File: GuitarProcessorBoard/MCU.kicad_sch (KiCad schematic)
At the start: 93 parts, among them J301 SWD Header, J302 PWR, J304 MODE, J305 BYP, J307 ScopeGroundLoop, SW301 RST, SW302 BOOT, U1 AMS1117, U301 STM32H7B0VBT6, U302 TPS63070, U303 SSD1306_OLED_128x64, U304 74HC595, Y301 32MHz, Y302 32.768kHZ

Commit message: migrated to new cube MX version, flashing on new board works
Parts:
- R314: value 5k1 -> 15k
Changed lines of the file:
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@@
 			)
 		)
-		(property "Value" "5k1"
+		(property "Value" "15k"
 			(at 249.555 241.3 0)
 			(effects

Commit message: updated schematic, re-annotated
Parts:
- removed C315, C317: 6p, Capacitor_SMD:C_0805_2012Metric, symbol Device:C
- removed C332: 100n, Capacitor_SMD:C_0805_2012Metric, symbol Device:C
- removed J302: PWR, Connector_PinHeader_2.54mm:PinHeader_1x04_P2.54mm_Vertical, symbol Connector:Conn_01x04_Pin
- removed R303, R304: 2k2, Resistor_SMD:R_0805_2012Metric, symbol Device:R_US
- removed U303: SSD1306_OLED_128x64, Display:SSD1306_OLED_128x64_OffBoard, symbol Display_Graphic:SSD1306_OLED_128x64
- removed Y302: 32.768kHZ, Crystal:Crystal_SMD_SeikoEpson_MC306-4Pin_8.0x3.2mm, symbol Device:Crystal_GND23
- added C37: 330u, Capacitor_THT:CP_Radial_D5.0mm_P2.50mm, symbol Device:C_Polarized_US
- added C48, C52: 10n, Capacitor_SMD:C_0805_2012Metric, symbol Device:C
- added J2: IO, Connector_PinHeader_2.54mm:PinHeader_1x06_P2.54mm_Vertical, symbol Connector:Conn_01x06_Pin
- added R24, R25, R39, R41: 47k, Resistor_SMD:R_0805_2012Metric, symbol Device:R_US
- added R36, R40: 22k, Resistor_SMD:R_0805_2012Metric, symbol Device:R_US
- added RV3, RV5: 100kB, Potentiometer_THT:Potentiometer_Alpha_RD901F-40-00D_Single_Vertical_CircularHoles, symbol Device:R_Potentiometer_US
- added SW3: SW_1, Button_Switch_THT:MiniToggle_SPST, symbol Switch:SW_SPST
- added SW4: SW_2, Button_Switch_THT:MiniToggle_SPST, symbol Switch:SW_SPST
- added TP4: OutL, TestPoint:TestPoint_THTPad_D2.0mm_Drill1.0mm_VAL, symbol Connector:TestPoint
- added TP5: OutR, TestPoint:TestPoint_THTPad_D2.0mm_Drill1.0mm_VAL, symbol Connector:TestPoint
- added TP7: DB1, TestPoint:TestPoint_THTPad_D2.0mm_Drill1.0mm_VAL, symbol Connector:TestPoint
- added TP8: DB2, TestPoint:TestPoint_THTPad_D2.0mm_Drill1.0mm_VAL, symbol Connector:TestPoint
- TP1: renamed from TP301; value In -> InL
- TP2: renamed from TP302; value Out -> InR
- renumbered C318 to C23, C301 to C24, C303 to C25, C302 to C26, C333 to C27, C304 to C28, C306 to C29, C307 to C30, C308 to C31, C309 to C32, C310 to C33, C311 to C34, C312 to C35, C313 to C36, C314 to C38, C2 to C39, C4 to C40, C3 to C41, C5 to C42, C6 to C43, C7 to C44, C329 to C45, C327 to C46, C319 to C47, C328 to C49, C321 to C50, C322 to C51, C323 to C53, C324 to C54, C326 to C55, C1 to C56, D304 to D1, D301 to D2, D307 to D3, D308 to D4, D309 to D5, D310 to D6, D311 to D7, D312 to D8, D302 to D9, J301 to J1, J307 to J3, J304 to J4, J305 to J5, L301 to L1, R309 to R21, R310 to R22, R305 to R23, R331 to R26, R333 to R27, R332 to R28, R330 to R29, R301 to R30, R302 to R31, R327 to R32, R328 to R33, R317 to R34, R315 to R35, R316 to R37, R311 to R38, R312 to R42, R313 to R43, R314 to R44, R306 to R45, R307 to R46, R308 to R47, R322 to R48, R323 to R49, R324 to R50, R325 to R51, R318 to R52, RV303 to RV1, RV301 to RV2, RV302 to RV4, SW301 to SW1, SW302 to SW2, TP303 to TP3, TP1 to TP6, U304 to U4, U301 to U5, U1 to U6, U302 to U7, Y301 to Y1
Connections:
- net +3.3V: now also R24.1, R25.1, RV3.3, RV5.3, SW3.2 (B), SW4.2 (B)
- net +9V: now also J2.5 (Pin_5)
- net GND: now also C37.2, C48.2, C52.2, J2.6 (Pin_6), R39.2, R41.2, RV3.1, RV5.1
- net VCC: now also C37.1
- net ADC_D: now reaches U5.22 (PA0)
- net ADC_D: now also C48.1, R36.2
- net ADC_E: now reaches U5.25 (PA3)
- net ADC_E: now also C52.1, R40.2
- net DBG1: now reaches U5.37 (PE7)
- net DBG1: now also R25.2, TP7.1
- net DBG2: now reaches U5.38 (PE8)
- net DBG2: now also R24.2, TP8.1
- net SWITCH2: now reaches U5.65 (PC8)
- net SWITCH2: now also R41.1, SW4.1 (A)
- net SWITCH1: now reaches U5.66 (PC9)
- net SWITCH1: now also R39.1, SW3.1 (A)
- net DISP_SCL: no longer names the net of U5.92 (PB6)
- net DISP_SDA: no longer names the net of U5.93 (PB7)
- net FX_IN renamed IN_L
- net IN_L: now also J2.3 (Pin_3)
- net FX_OUT renamed IN_R
- net IN_R: now also J2.4 (Pin_4)
- net LFE_IN: no longer names the net of U5.9 (PC15)
- net LFE_OUT: no longer names the net of U5.8 (PC14)
- new net: R40.1, RV5.2
- new net: R36.1, RV3.2
- new net OUT_L: J2.1 (Pin_1), TP4.1
- new net OUT_R: J2.2 (Pin_2), TP5.1
- no-connect marks 57 -> 55
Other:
- note removed: "LFE Crystal"
- moved on the sheet: C40, C42, C43, C44, C47, C50, C51, C53, C54, C55, C56, D1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

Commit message: new layout
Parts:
- removed C23: 100n, Capacitor_SMD:C_0805_2012Metric, symbol Device:C
- removed C38: 2u2, Capacitor_SMD:C_0805_2012Metric, symbol Device:C
- removed C39: 10u, Capacitor_SMD:C_0805_2012Metric, symbol Device:C
- removed C52: 10n, Capacitor_SMD:C_0805_2012Metric, symbol Device:C
- removed R24, R25, R41: 47k, Resistor_SMD:R_0805_2012Metric, symbol Device:R_US
- removed R40: 22k, Resistor_SMD:R_0805_2012Metric, symbol Device:R_US
- removed RV5: 100kB, Potentiometer_THT:Potentiometer_Alpha_RD901F-40-00D_Single_Vertical_CircularHoles, symbol Device:R_Potentiometer_US
- removed SW2: BOOT, Button_Switch_SMD:SW_SPST_B3U-1000P, symbol Switch:SW_SPST
- removed SW4: SW_2, Button_Switch_THT:MiniToggle_SPST, symbol Switch:SW_SPST
- J3: footprint Connector:THT_GND_WIRE -> Capacitor_THT:THT_GND_WIRE
- U7: footprint Package_DFN_QFN:TXN_QFN15 -> Converter_DCDC:TXN_QFN15
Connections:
- net DBG1: now also U5.82 (PD1); no longer U5.37 (PE7)
- net DBG2: now also U5.83 (PD2); no longer U5.38 (PE8)
- net LED_BYPASS: now also U4.6 (QG); no longer U4.7 (QH)
- net LED_TEMPO: now also U4.7 (QH); no longer U4.6 (QG)
- net ADC_E: no longer names the net of U5.25 (PA3)
- net SWITCH2: no longer names the net of U5.65 (PC8)
- no-connect marks 55 -> 57
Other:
- moved on the sheet: C41, SW1

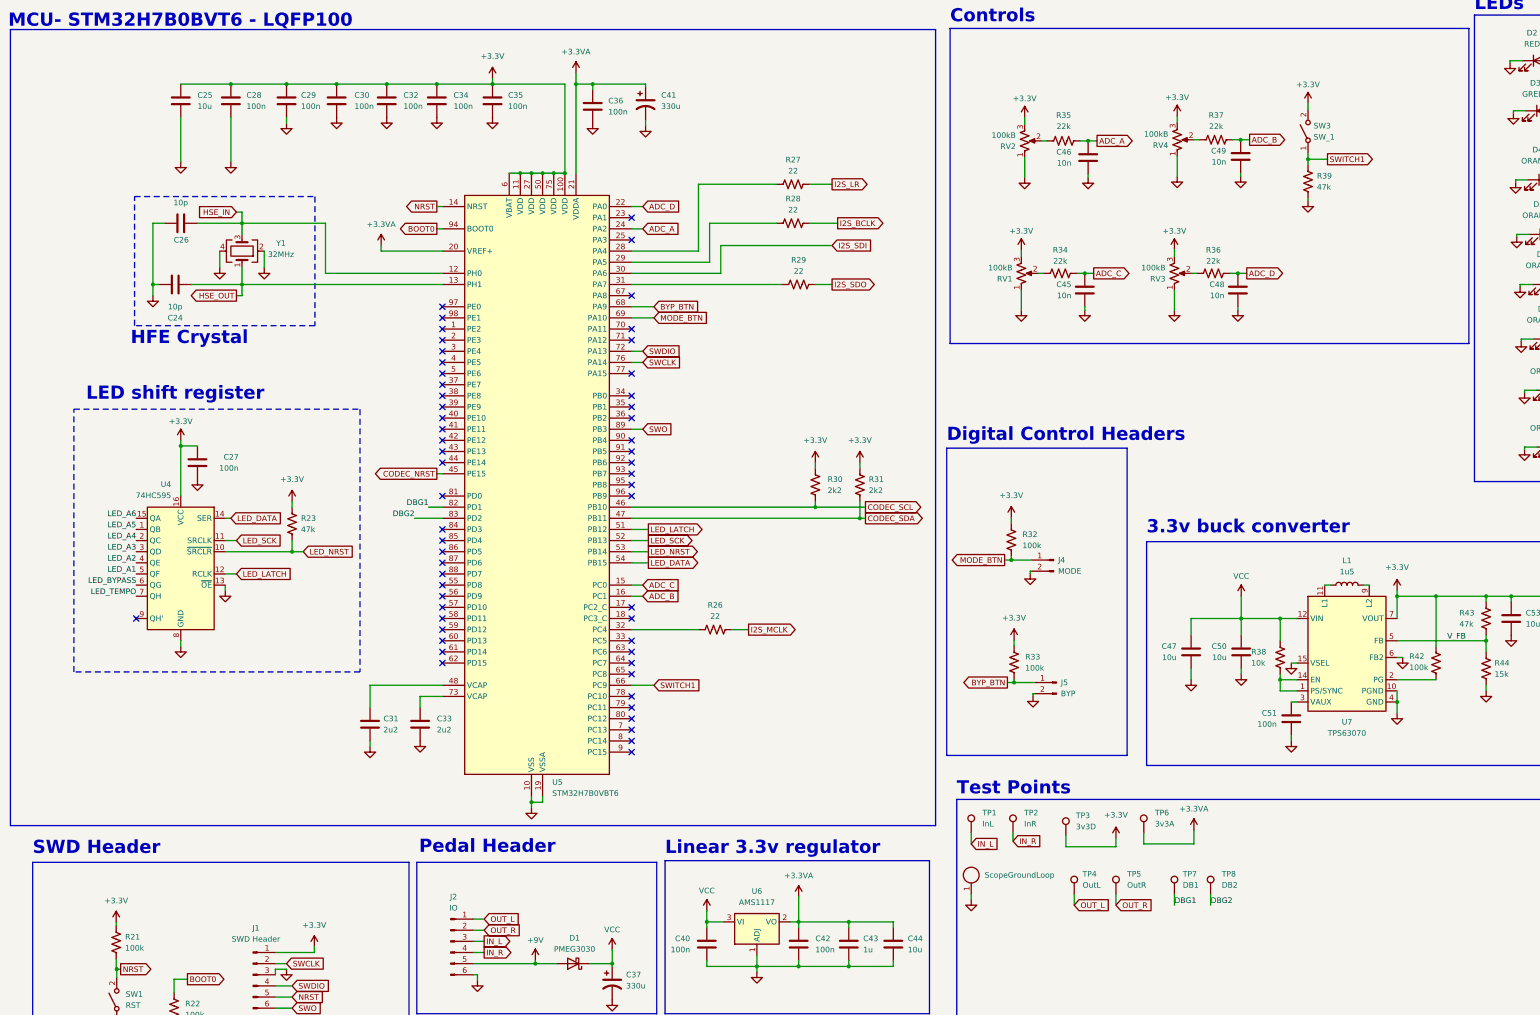
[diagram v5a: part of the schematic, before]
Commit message: prelim. routing, DRC passing
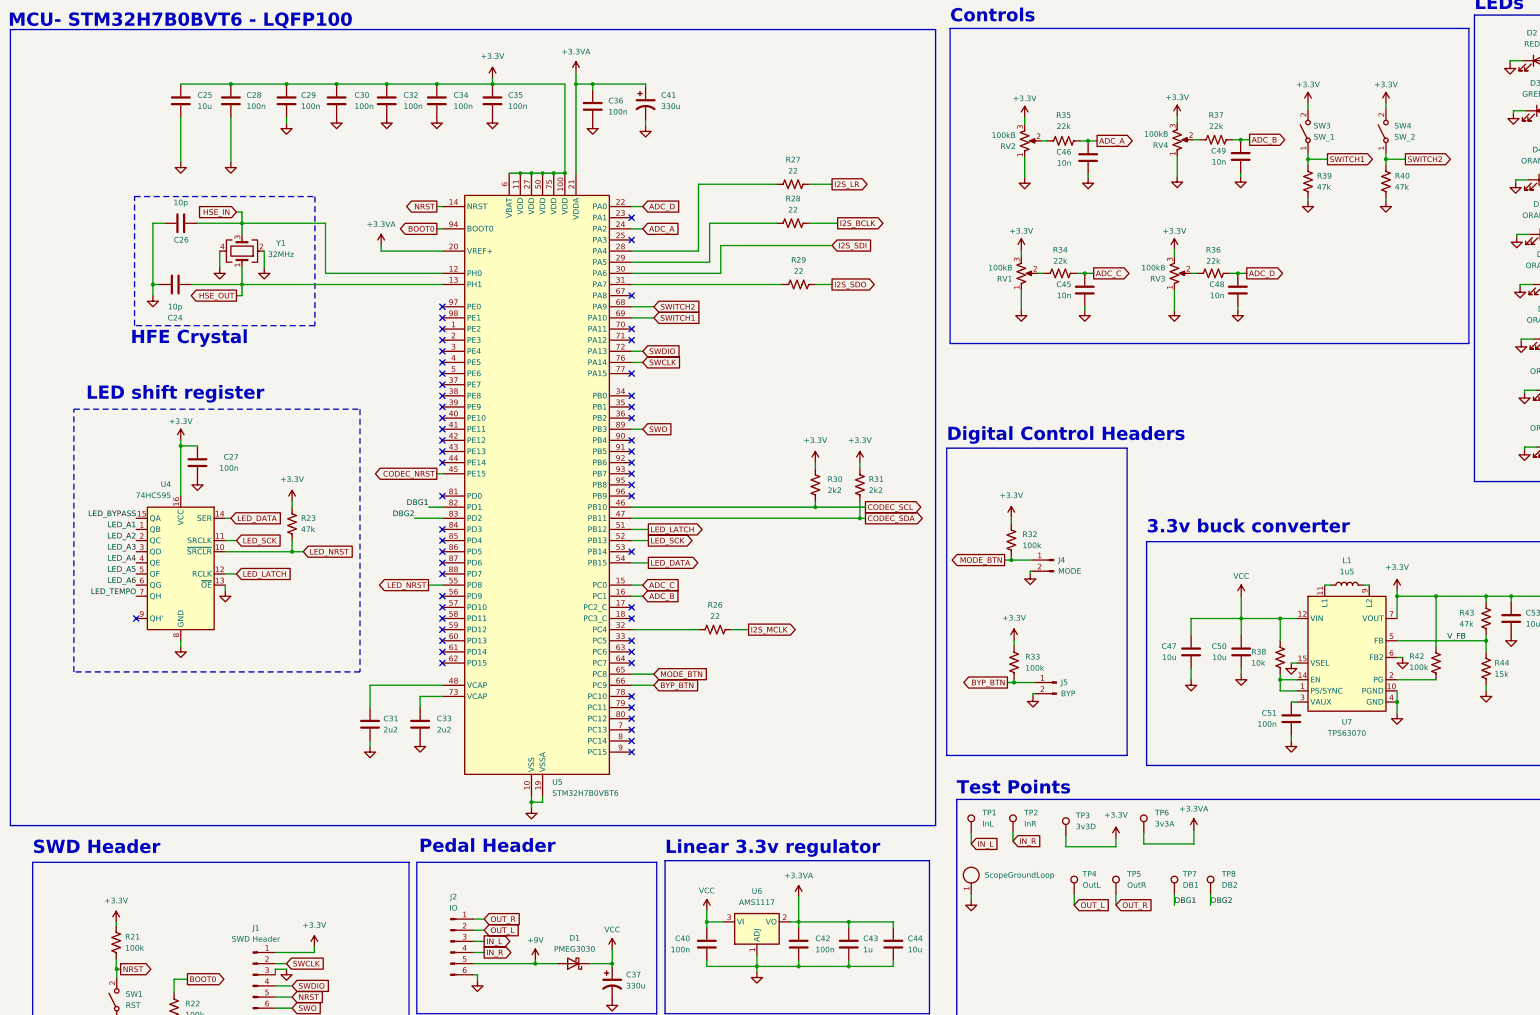
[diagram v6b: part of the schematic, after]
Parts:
- added R40: 47k, Resistor_SMD:R_0805_2012Metric, symbol Device:R_US
- added SW4: SW_2, Button_Switch_THT:MiniToggle_SPST, symbol Switch:SW_SPST
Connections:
- net +3.3V: now also SW4.2 (B)
- net BYP_BTN: now also U5.66 (PC9); no longer U5.68 (PA9)
- net GND: now also R40.2
- net LED_A1: now also U4.1 (QB); no longer U4.5 (QF)
- net LED_A2: now also U4.2 (QC); no longer U4.4 (QE)
- net LED_A4: now also U4.4 (QE); no longer U4.2 (QC)
- net LED_A5: now also U4.5 (QF); no longer U4.1 (QB)
- net LED_A6: now also U4.6 (QG); no longer U4.15 (QA)
- net LED_BYPASS: now also U4.15 (QA); no longer U4.6 (QG)
- net LED_NRST: now also U5.55 (PD8); no longer U5.53 (PB14)
- net MODE_BTN: now also U5.65 (PC8); no longer U5.69 (PA10)
- net OUT_L: now also J2.2 (Pin_2); no longer J2.1 (Pin_1)
- net OUT_R: now also J2.1 (Pin_1); no longer J2.2 (Pin_2)
- net SWITCH1: now also U5.69 (PA10); no longer U5.66 (PC9)
- new net SWITCH2: R40.1, SW4.1 (A), U5.68 (PA9)
- no-connect marks 57 -> 56

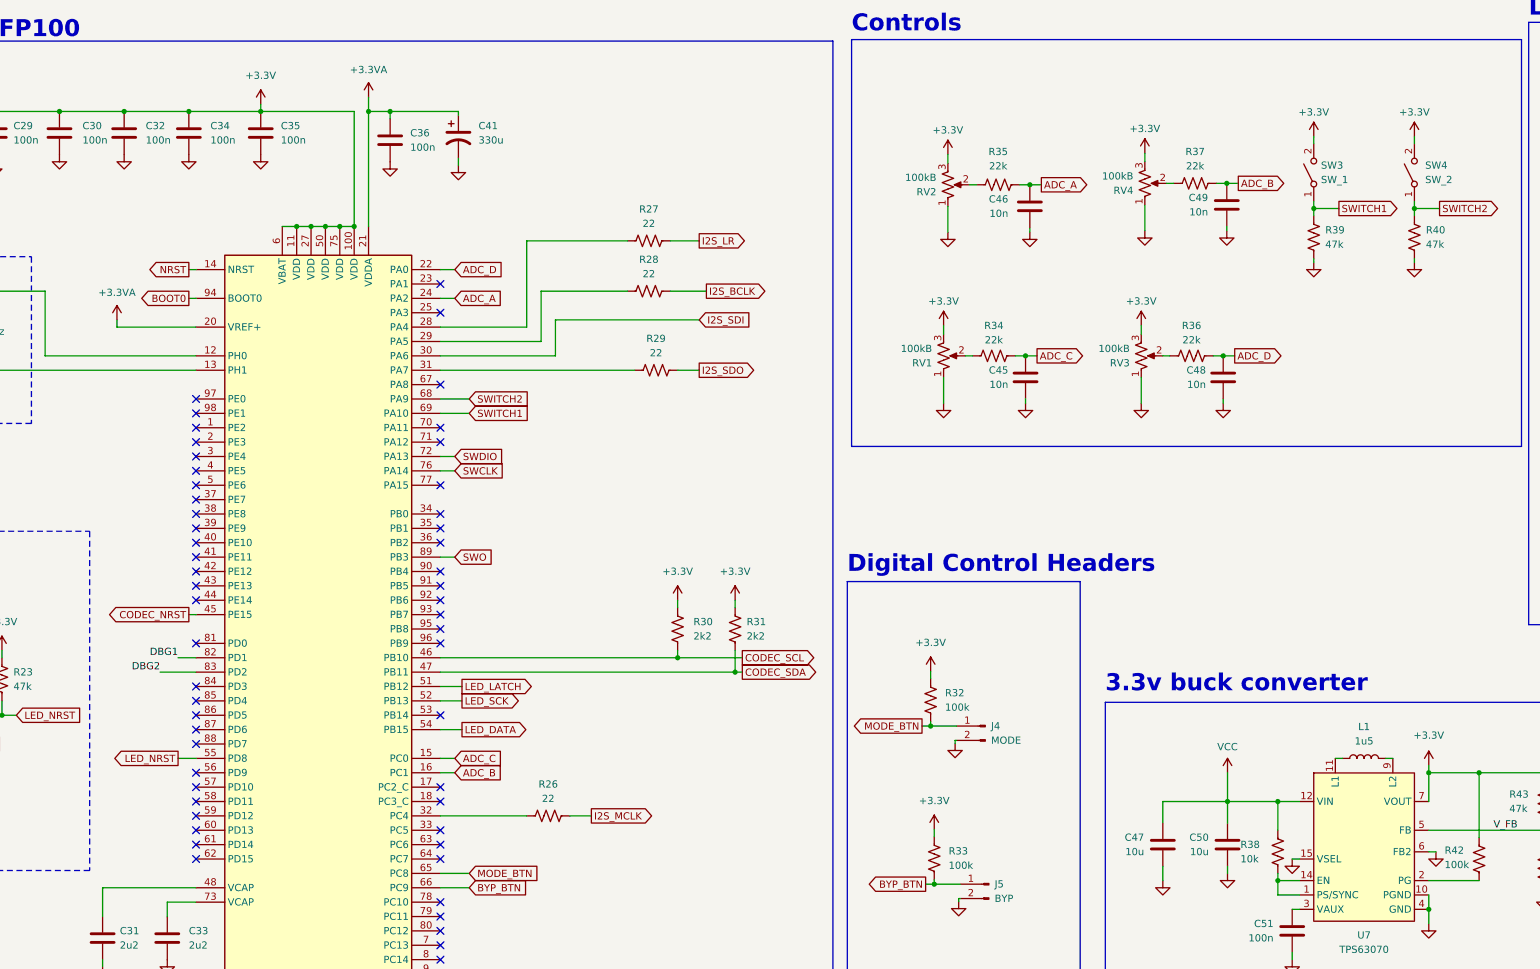
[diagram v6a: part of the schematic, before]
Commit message: new layout, pinout switcharoo
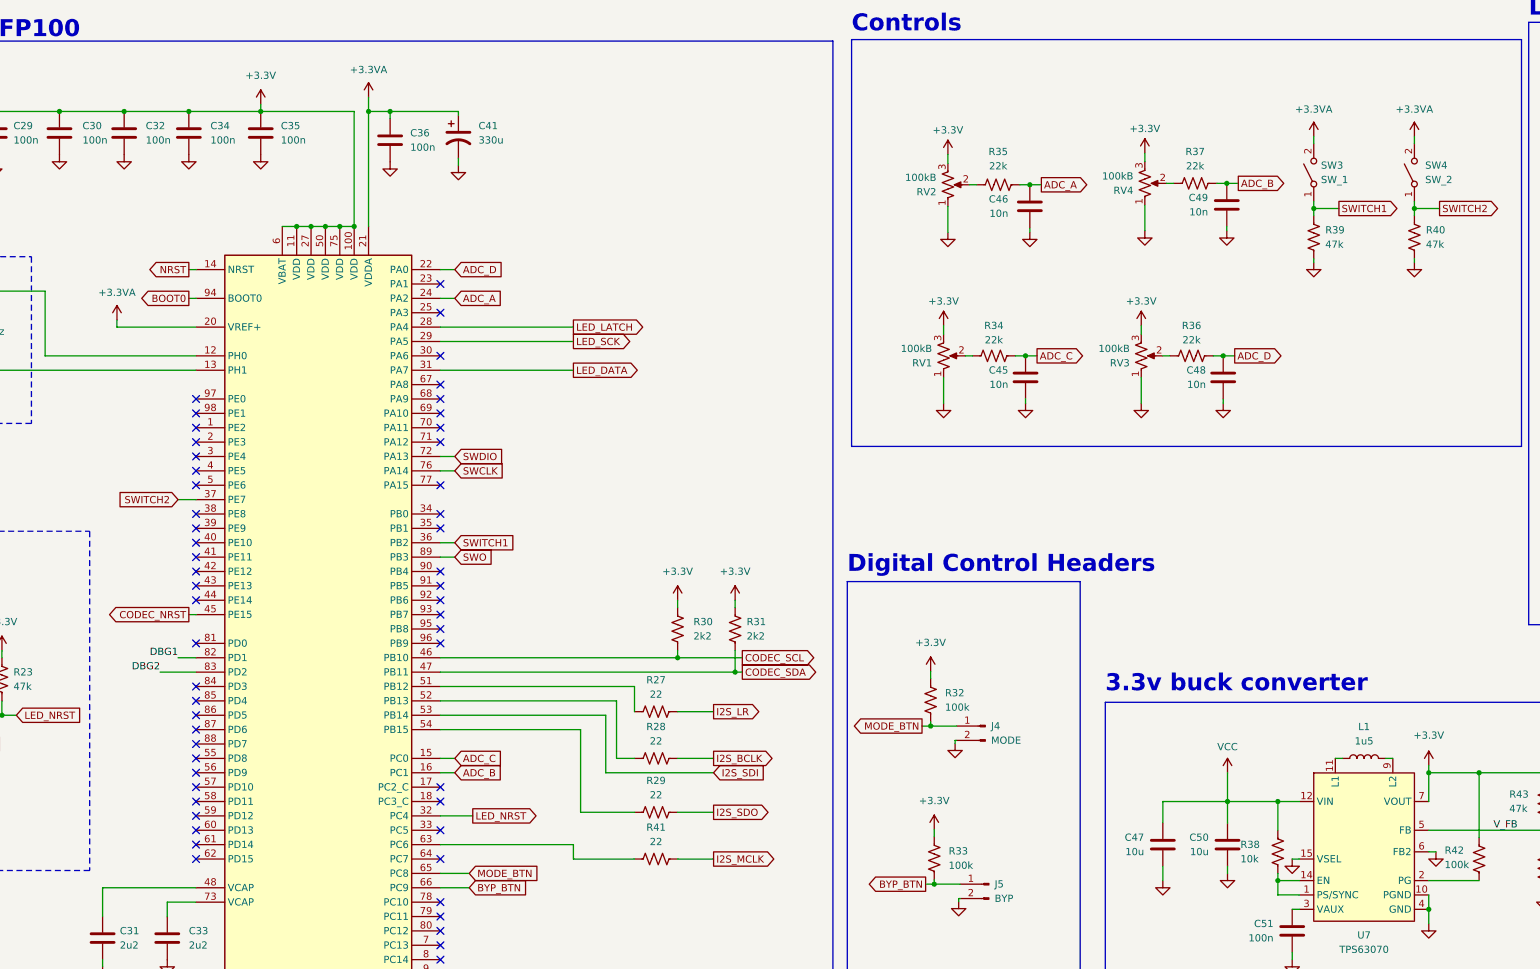
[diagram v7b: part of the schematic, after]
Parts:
- removed R26: 22, Resistor_SMD:R_0805_2012Metric, symbol Device:R_US
- added R41: 22, Resistor_SMD:R_0805_2012Metric, symbol Device:R_US
- J3: footprint Capacitor_THT:THT_GND_WIRE -> Connector:THT_GND_WIRE
- U7: footprint Converter_DCDC:TXN_QFN15 -> Converter_DCDC:Converter_DCDC_TXN_QFN15
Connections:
- net +3.3V: no longer SW3.2 (B), SW4.2 (B)
- net +3.3VA: now also SW3.2 (B), SW4.2 (B)
- net I2S_MCLK: now also R41.2
- net I2S_SDI: now also U5.53 (PB14); no longer U5.30 (PA6)
- net LED_DATA: now also U5.31 (PA7); no longer U5.54 (PB15)
- net LED_LATCH: now also U5.28 (PA4); no longer U5.51 (PB12)
- net LED_NRST: now also U5.32 (PC4); no longer U5.55 (PD8)
- net LED_SCK: now also U5.29 (PA5); no longer U5.52 (PB13)
- net SWITCH1: now also U5.36 (PB2); no longer U5.69 (PA10)
- net SWITCH2: now also U5.37 (PE7); no longer U5.68 (PA9)
- net at R27.1: now also U5.51 (PB12); no longer U5.28 (PA4)
- net at R28.1: now also U5.52 (PB13); no longer U5.29 (PA5)
- net at R29.1: now also U5.54 (PB15); no longer U5.31 (PA7)
- net at U5.63 (PC6): now also R41.1
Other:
- moved on the sheet: R27, R28, R29

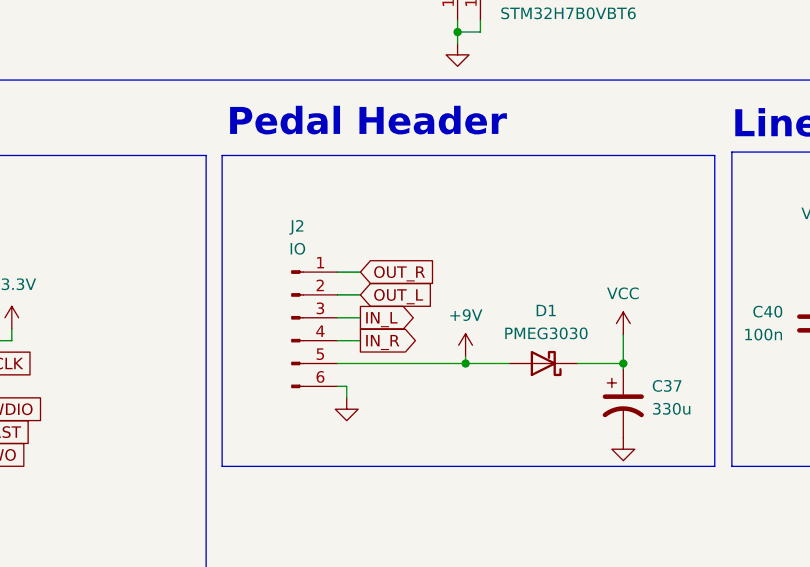
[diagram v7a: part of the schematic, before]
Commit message: prelim routing, DRC passing
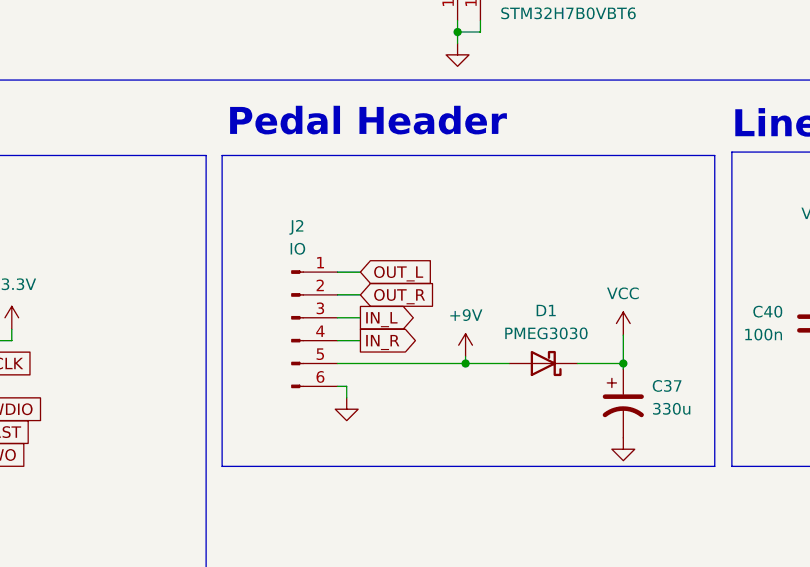
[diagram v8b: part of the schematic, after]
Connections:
- net OUT_L: now also J2.1 (Pin_1); no longer J2.2 (Pin_2)
- net OUT_R: now also J2.2 (Pin_2); no longer J2.1 (Pin_1)
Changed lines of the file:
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@@
 	(global_label "OUT_R"
 		(shape input)
-		(at 126.365 224.79 0)
+		(at 126.365 227.33 0)
 		(fields_autoplaced yes)
 		(effects
@@
 		)
 		(property "Intersheetrefs" "${INTERSHEET_REFS}"
-			(at 135.2164 224.79 0)
+			(at 135.2164 227.33 0)
 			(hide yes)
 			(show_name no)
@@
 	(global_label "OUT_L"
 		(shape input)
-		(at 126.365 227.33 0)
+		(at 126.365 224.79 0)
 		(fields_autoplaced yes)
 		(effects
@@
 		)
 		(property "Intersheetrefs" "${INTERSHEET_REFS}"
-			(at 134.9745 227.33 0)
+			(at 134.9745 224.79 0)
 			(hide yes)
 			(show_name no)
